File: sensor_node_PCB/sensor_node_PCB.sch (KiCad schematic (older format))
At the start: 17 parts

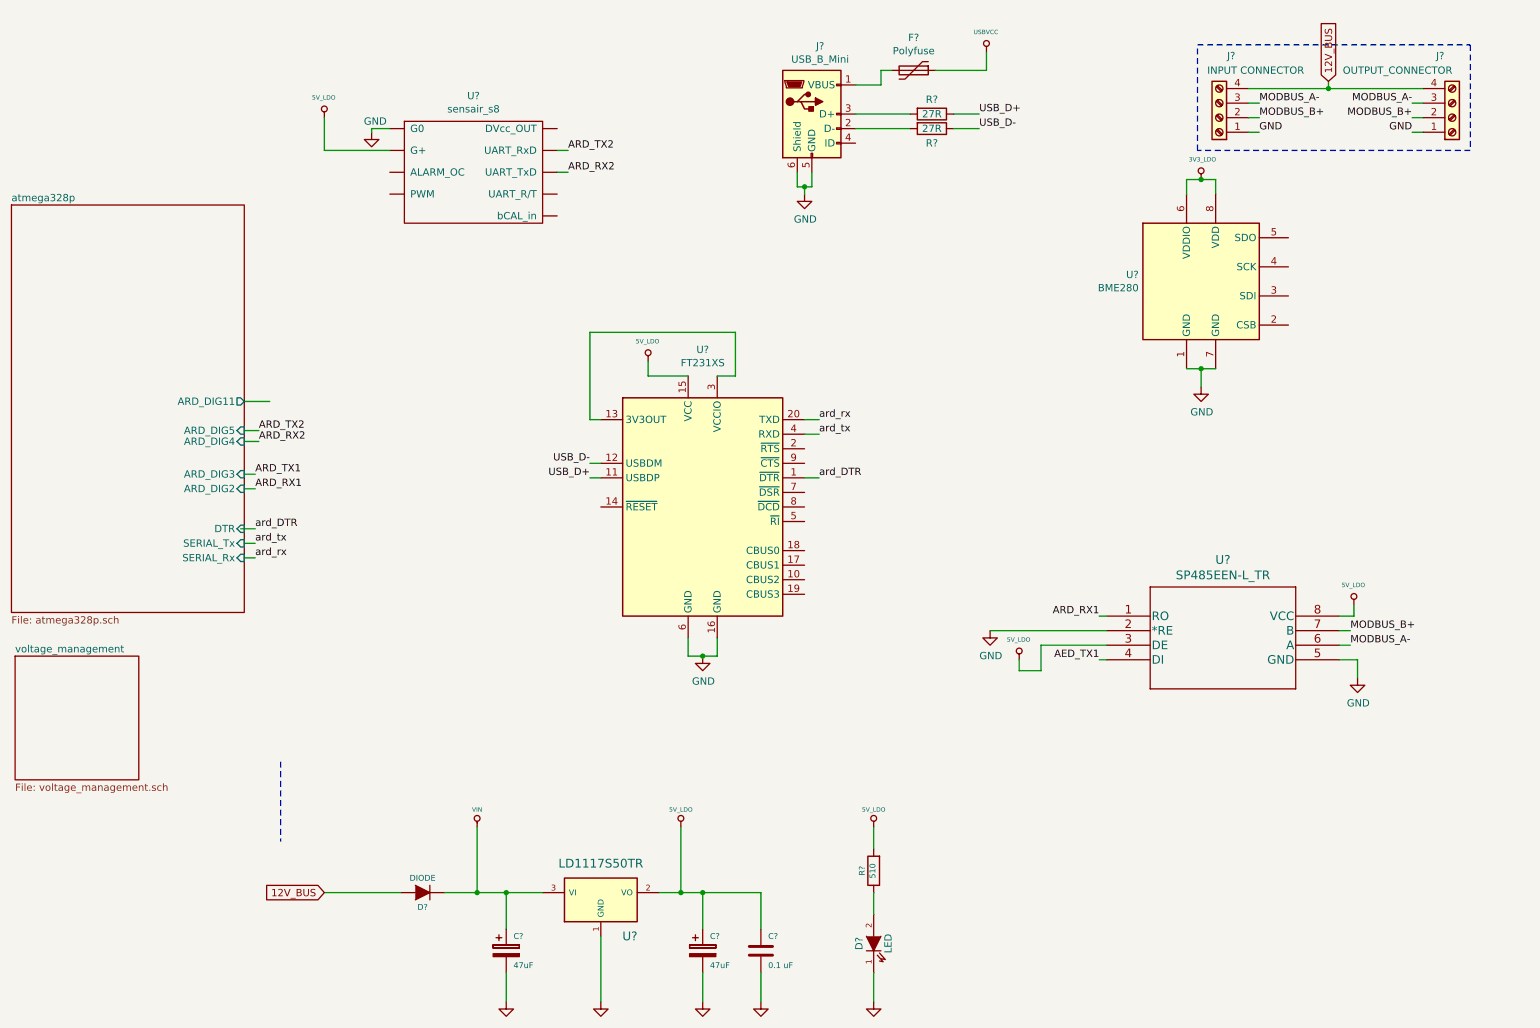
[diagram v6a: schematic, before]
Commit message: added level shifter for bme280
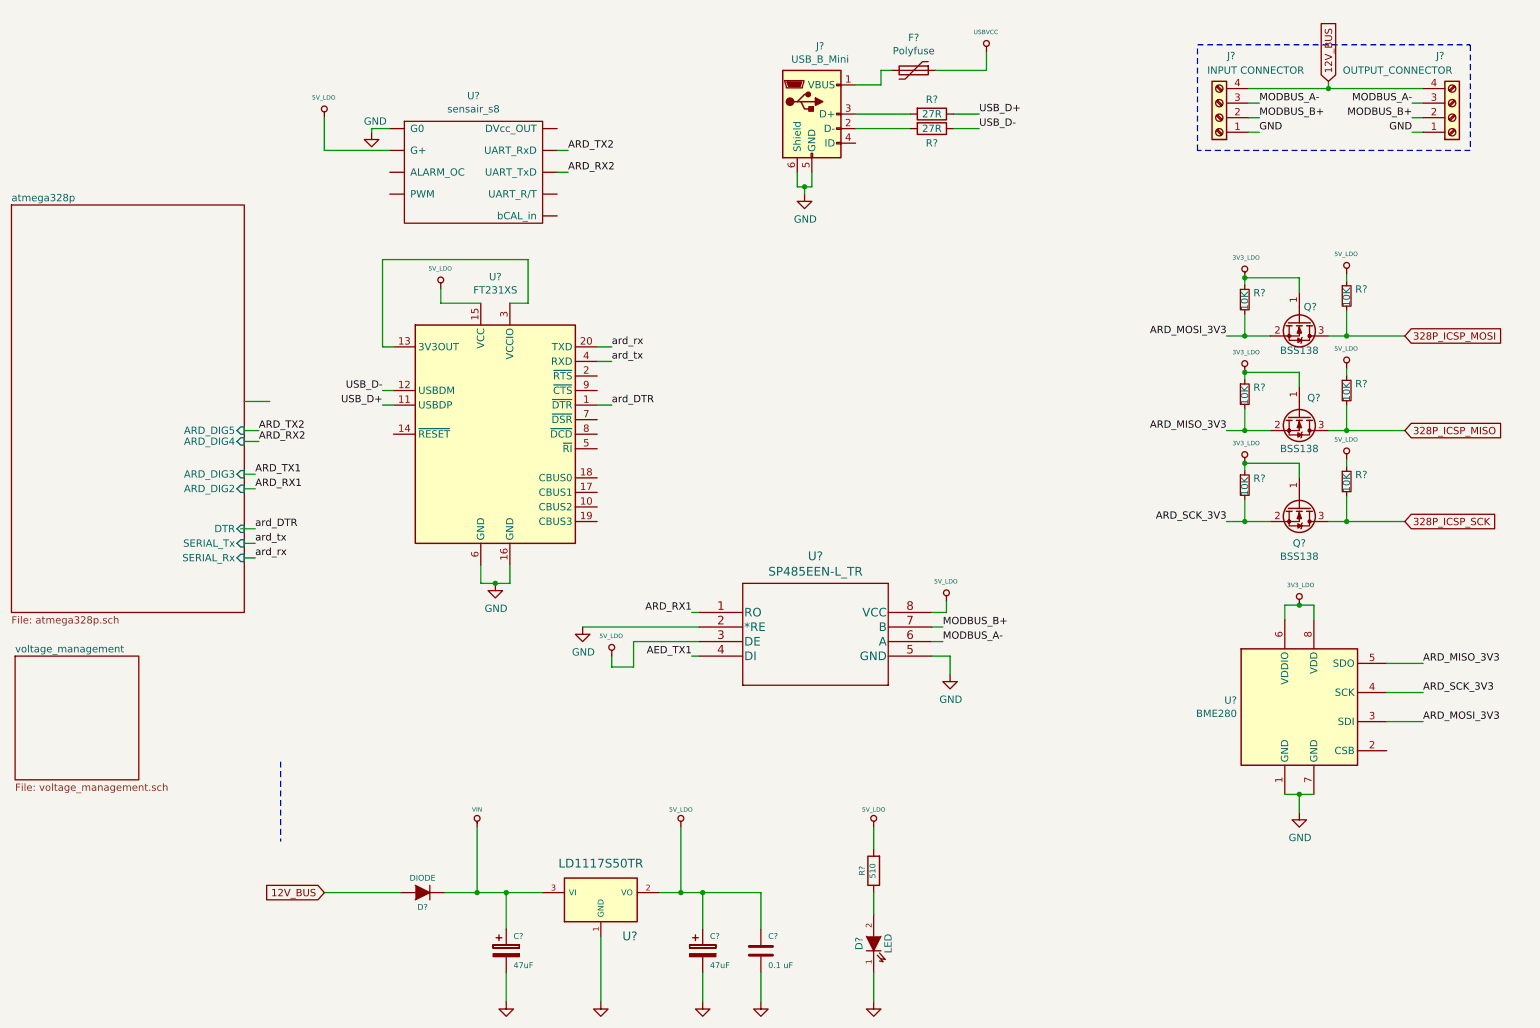
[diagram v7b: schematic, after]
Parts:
- added Q? (x3): BSS138, Package_TO_SOT_SMD:SOT-23, symbol Transistor_FET:BSS138
- added R? (x6): 10K, symbol Device:R_Small
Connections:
- net 3V3_LDO: now also Q?.1 (G), Q?.1 (G), Q?.1 (G), R?.1, R?.1, R?.1
- net 5V_LDO: now also R?.1, R?.1, R?.1
- net ARD_MOSI_3V3: now reaches U?.3 (SDI)
- net ARD_MOSI_3V3: now also Q?.2 (S), R?.2
- net ARD_SCK_3V3: now reaches U?.4 (SCK)
- net ARD_SCK_3V3: now also Q?.2 (S), R?.2
- net ARD_MISO_3V3: now reaches U?.5 (SDO)
- net ARD_MISO_3V3: now also Q?.2 (S), R?.2
- new net 328P_ICSP_MISO: Q?.3 (D), R?.2
- new net 328P_ICSP_MOSI: Q?.3 (D), R?.2
- new net 328P_ICSP_SCK: Q?.3 (D), R?.2
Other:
- moved on the sheet: U?

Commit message: changed bme280 to use i2c
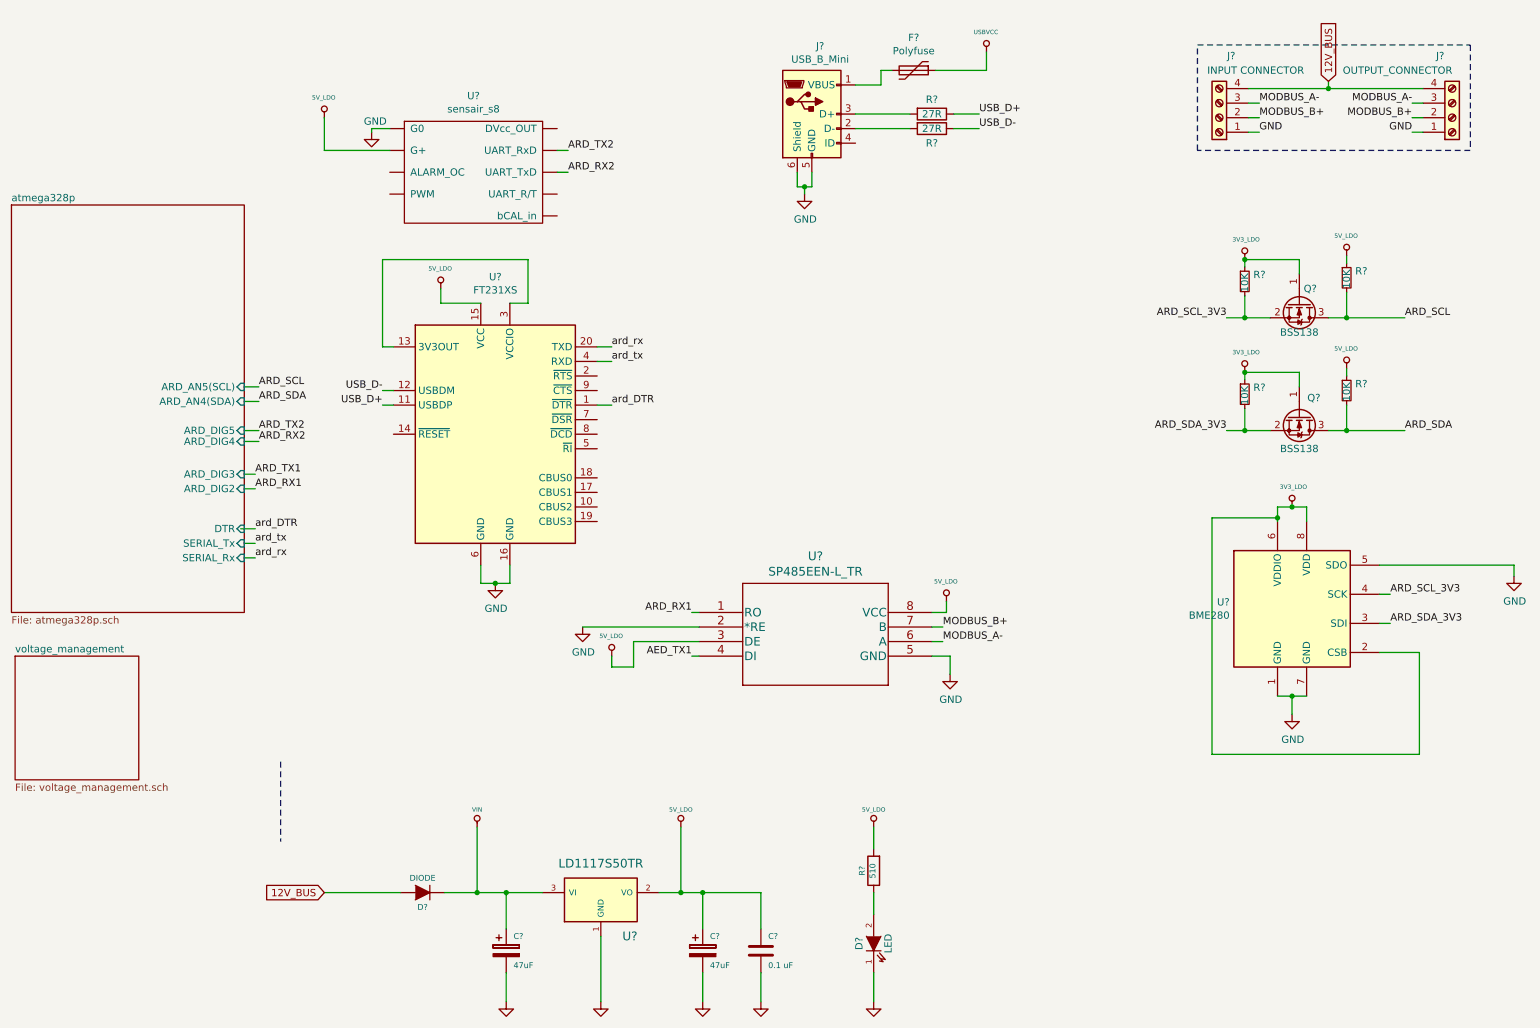
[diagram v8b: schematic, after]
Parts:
- removed Q?: BSS138, Package_TO_SOT_SMD:SOT-23, symbol Transistor_FET:BSS138
- removed R? (x2): 10K, symbol Device:R_Small
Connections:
- net ARD_SCK_3V3 is gone; now on net ARD_SCL_3V3: U?.4 (SCK)
- net 3V3_LDO: now also U?.2 (CSB)
- net GND: now also U?.5 (SDO)
- net 328P_ICSP_MISO renamed ARD_SDA
- net 328P_ICSP_MOSI renamed ARD_SCL
- net ARD_MISO_3V3 renamed ARD_SDA_3V3
- net ARD_SDA_3V3: now also U?.3 (SDI); no longer U?.5 (SDO)
- net ARD_MOSI_3V3 renamed ARD_SCL_3V3
- net ARD_SCL_3V3: no longer U?.3 (SDI)
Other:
- moved on the sheet: Q?, R?, U?
